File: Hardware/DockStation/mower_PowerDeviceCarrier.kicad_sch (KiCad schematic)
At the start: 5 parts, among them J1 Conn_01x04, J2 Conn_01x04

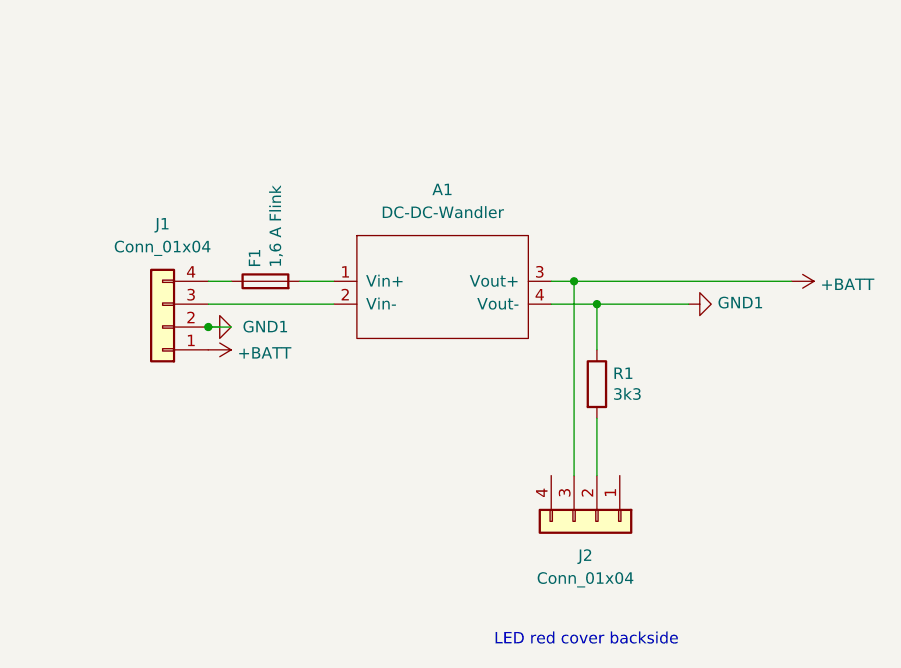
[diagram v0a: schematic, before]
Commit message: feat(dock): add 3.81mm terminals and pinholes to connect to dc/dc terminal
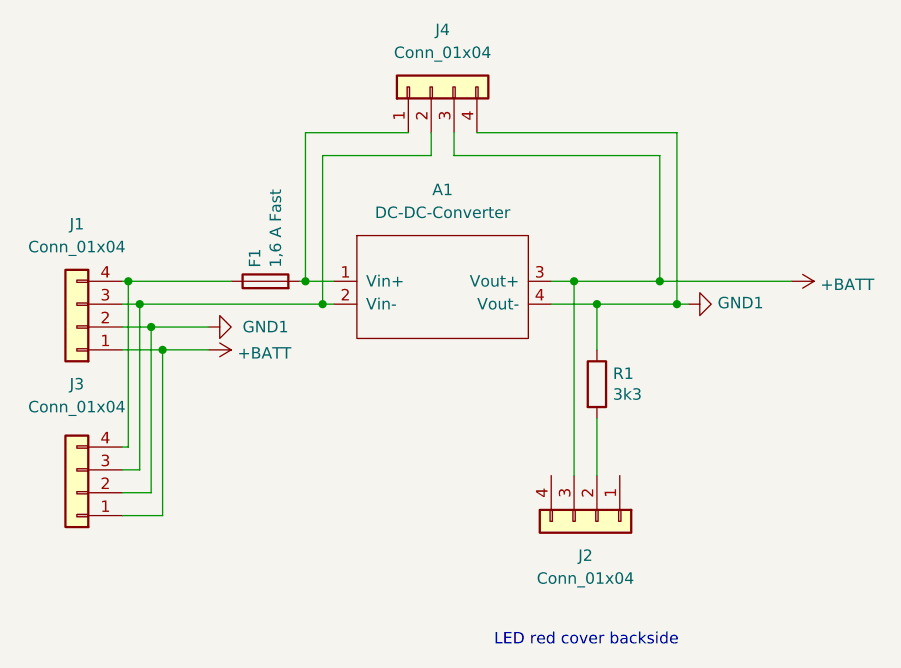
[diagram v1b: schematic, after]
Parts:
- added J3: Conn_01x04, Connector_Phoenix_MC:PhoenixContact_MCV_1,5_4-G-3.81_1x04_P3.81mm_Vertical, symbol ene9ba_library:Conn_01x04
- added J4: Conn_01x04, Connector_PinHeader_2.54mm:PinHeader_1x07_P2.54mm_Vertical, symbol Connector_Generic:Conn_01x04
- A1: value DC-DC-Wandler -> DC-DC-Converter
- F1: value 1,6 A Flink -> 1,6 A Fast
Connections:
- net +BATT: now also J3.1 (Pin_1), J4.3 (Pin_3)
- net GND1: now also J3.2 (Pin_2), J4.4 (Pin_4)
- net at F1.1, J1.4 (Pin_4): now also J3.4 (Pin_4)
- net at A1.1 (Vin+), F1.2: now also J4.1 (Pin_1)
- net at A1.2 (Vin-), J1.3 (Pin_3): now also J3.3 (Pin_3), J4.2 (Pin_2)
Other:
- moved on the sheet: J1
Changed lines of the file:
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@@
 (kicad_sch (version 20211123) (generator eeschema)
   (paper "A4")
+  (junction (at 100.33 77.47) (diameter 0) (color 0 0 0 0)
+  )
   (junction (at 151.13 77.47) (diameter 0) (color 0 0 0 0)
   )
+  (junction (at 99.06 74.93) (diameter 0) (color 0 0 0 0)
+  )
+  (junction (at 102.87 82.55) (diameter 0) (color 0 0 0 0)
+  )
+  (junction (at 120.65 77.47) (diameter 0) (color 0 0 0 0)
+  )
+  (junction (at 118.745 74.93) (diameter 0) (color 0 0 0 0)
+  )
+  (junction (at 160.02 77.47) (diameter 0) (color 0 0 0 0)
+  )
+  (junction (at 158.115 74.93) (diameter 0) (color 0 0 0 0)
+  )
   (junction (at 148.59 74.93) (diameter 0) (color 0 0 0 0)
   )
-  (junction (at 107.95 80.01) (diameter 0) (color 0 0 0 0)
+  (junction (at 101.6 80.01) (diameter 0) (color 0 0 0 0)
+  )
+  (wire (pts (xy 135.255 60.96) (xy 158.115 60.96))
+    (stroke (width 0) (type default) (color 0 0 0 0))
+  )
+  (wire (pts (xy 130.175 58.42) (xy 118.745 58.42))
+    (stroke (width 0) (type default) (color 0 0 0 0))
+  )
+  (wire (pts (xy 132.715 60.96) (xy 120.65 60.96))
+    (stroke (width 0) (type default) (color 0 0 0 0))
+  )
+  (wire (pts (xy 160.02 58.42) (xy 160.02 77.47))
+    (stroke (width 0) (type default) (color 0 0 0 0))
   )
   (wire (pts (xy 151.13 77.47) (xy 151.13 82.55))
     (stroke (width 0) (type default) (color 0 0 0 0))
   )
-  (wire (pts (xy 118.11 74.93) (xy 121.92 74.93))
-    (stroke (width 0) (type default) (color 0 0 0 0))
-  )
-  (wire (pts (xy 148.59 74.93) (xy 172.72 74.93))
+  (wire (pts (xy 118.11 74.93) (xy 118.745 74.93))
+    (stroke (width 0) (type default) (color 0 0 0 0))
+  )
+  (wire (pts (xy 98.425 98.425) (xy 101.6 98.425))
+    (stroke (width 0) (type default) (color 0 0 0 0))
+  )
+  (wire (pts (xy 148.59 74.93) (xy 158.115 74.93))
+    (stroke (width 0) (type default) (color 0 0 0 0))
+  )
+  (wire (pts (xy 100.33 95.885) (xy 100.33 77.47))
+    (stroke (width 0) (type default) (color 0 0 0 0))
+  )
+  (wire (pts (xy 98.425 100.965) (xy 102.87 100.965))
     (stroke (width 0) (type default) (color 0 0 0 0))
   )
@@
     (stroke (width 0) (type default) (color 0 0 0 0))
   )
-  (wire (pts (xy 107.95 74.93) (xy 110.49 74.93))
+  (wire (pts (xy 98.425 95.885) (xy 100.33 95.885))
+    (stroke (width 0) (type default) (color 0 0 0 0))
+  )
+  (wire (pts (xy 99.06 93.345) (xy 99.06 74.93))
+    (stroke (width 0) (type default) (color 0 0 0 0))
+  )
+  (wire (pts (xy 120.65 77.47) (xy 121.92 77.47))
+    (stroke (width 0) (type default) (color 0 0 0 0))
+  )
+  (wire (pts (xy 98.425 82.55) (xy 102.87 82.55))
+    (stroke (width 0) (type default) (color 0 0 0 0))
+  )
+  (wire (pts (xy 100.33 77.47) (xy 120.65 77.47))
+    (stroke (width 0) (type default) (color 0 0 0 0))
+  )
+  (wire (pts (xy 98.425 74.93) (xy 99.06 74.93))
+    (stroke (width 0) (type default) (color 0 0 0 0))
+  )
+  (wire (pts (xy 132.715 58.42) (xy 132.715 60.96))
     (stroke (width 0) (type default) (color 0 0 0 0))
   )
@@
     (stroke (width 0) (type default) (color 0 0 0 0))
   )
-  (wire (pts (xy 107.95 80.01) (xy 110.49 80.01))
-    (stroke (width 0) (type default) (color 0 0 0 0))
-  )
-  (wire (pts (xy 151.13 77.47) (xy 161.29 77.47))
+  (wire (pts (xy 99.06 74.93) (xy 110.49 74.93))
+    (stroke (width 0) (type default) (color 0 0 0 0))
+  )
+  (wire (pts (xy 158.115 60.96) (xy 158.115 74.93))
+    (stroke (width 0) (type default) (color 0 0 0 0))
+  )
+  (wire (pts (xy 135.255 58.42) (xy 135.255 60.96))
+    (stroke (width 0) (type default) (color 0 0 0 0))
+  )
+  (wire (pts (xy 120.65 60.96) (xy 120.65 77.47))
+    (stroke (width 0) (type default) (color 0 0 0 0))
+  )
+  (wire (pts (xy 98.425 80.01) (xy 101.6 80.01))
+    (stroke (width 0) (type default) (color 0 0 0 0))
+  )
+  (wire (pts (xy 101.6 80.01) (xy 107.95 80.01))
+    (stroke (width 0) (type default) (color 0 0 0 0))
+  )
+  (wire (pts (xy 102.87 82.55) (xy 107.95 82.55))
+    (stroke (width 0) (type default) (color 0 0 0 0))
+  )
+  (wire (pts (xy 151.13 77.47) (xy 160.02 77.47))
+    (stroke (width 0) (type default) (color 0 0 0 0))
+  )
+  (wire (pts (xy 158.115 74.93) (xy 172.72 74.93))
+    (stroke (width 0) (type default) (color 0 0 0 0))
+  )
+  (wire (pts (xy 137.795 58.42) (xy 160.02 58.42))
+    (stroke (width 0) (type default) (color 0 0 0 0))
+  )
+  (wire (pts (xy 101.6 98.425) (xy 101.6 80.01))
+    (stroke (width 0) (type default) (color 0 0 0 0))
+  )
+  (wire (pts (xy 102.87 100.965) (xy 102.87 82.55))
     (stroke (width 0) (type default) (color 0 0 0 0))
   )
@@
     (stroke (width 0) (type default) (color 0 0 0 0))
   )
-  (wire (pts (xy 107.95 77.47) (xy 121.92 77.47))
+  (wire (pts (xy 118.745 74.93) (xy 121.92 74.93))
+    (stroke (width 0) (type default) (color 0 0 0 0))
+  )
+  (wire (pts (xy 160.02 77.47) (xy 161.29 77.47))
+    (stroke (width 0) (type default) (color 0 0 0 0))
+  )
+  (wire (pts (xy 98.425 93.345) (xy 99.06 93.345))
+    (stroke (width 0) (type default) (color 0 0 0 0))
+  )
+  (wire (pts (xy 118.745 58.42) (xy 118.745 74.93))
+    (stroke (width 0) (type default) (color 0 0 0 0))
+  )
+  (wire (pts (xy 98.425 77.47) (xy 100.33 77.47))
     (stroke (width 0) (type default) (color 0 0 0 0))
   )
@@
       (effects (font (size 1.27 1.27)) (justify left))
     )
-    (property "Value" "1,6 A Flink" (id 1) (at 115.443 73.406 0)
+    (property "Value" "1,6 A Fast" (id 1) (at 115.443 73.406 0)
       (effects (font (size 1.27 1.27)) (justify left))
     )
@@
     (pin "1")
   )
-  (symbol (lib_id "ene9ba_library:Conn_01x04") (at 102.87 80.01 180) (unit 1)
-    (in_bom yes) (on_board yes) (fields_autoplaced)
-    (property "Reference" "J1" (id 0) (at 102.87 68.58 0))
-    (property "Value" "Conn_01x04" (id 1) (at 102.87 71.12 0))
-    (property "Footprint" "Connector_Phoenix_MSTB:PhoenixContact_MSTBVA_2,5_4-G-5,08_1x04_P5.08mm_Vertical" (id 2) (at 102.87 80.01 0)
-      (effects (font (size 1.27 1.27)) hide)
-    )
-    (property "Datasheet" "" (id 3) (at 102.87 80.01 0)
+  (symbol (lib_id "ene9ba_library:Conn_01x04") (at 93.345 98.425 180) (unit 1)
+    (in_bom yes) (on_board yes) (fields_autoplaced)
+    (property "Reference" "J3" (id 0) (at 93.345 86.36 0))
+    (property "Value" "Conn_01x04" (id 1) (at 93.345 88.9 0))
+    (property "Footprint" "Connector_Phoenix_MC:PhoenixContact_MCV_1,5_4-G-3.81_1x04_P3.81mm_Vertical" (id 2) (at 93.345 98.425 0)
+      (effects (font (size 1.27 1.27)) hide)
+    )
+    (property "Datasheet" "" (id 3) (at 93.345 98.425 0)
+      (effects (font (size 1.27 1.27)) hide)
+    )
+    (pin "1")
+    (pin "2")
+    (pin "3")
+    (pin "4")
+  )
+  (symbol (lib_id "Connector_Generic:Conn_01x04") (at 132.715 53.34 90) (unit 1)
+    (in_bom yes) (on_board yes) (fields_autoplaced)
+    (property "Reference" "J4" (id 0) (at 133.985 46.99 90))
+    (property "Value" "Conn_01x04" (id 1) (at 133.985 49.53 90))
+    (property "Footprint" "Connector_PinHeader_2.54mm:PinHeader_1x07_P2.54mm_Vertical" (id 2) (at 132.715 53.34 0)
+      (effects (font (size 1.27 1.27)) hide)
+    )
+    (property "Datasheet" "~" (id 3) (at 132.715 53.34 0)
+      (effects (font (size 1.27 1.27)) hide)
+    )
+    (pin "1")
+    (pin "2")
+    (pin "3")
+    (pin "4")
+  )
+  (symbol (lib_id "ene9ba_library:Conn_01x04") (at 93.345 80.01 180) (unit 1)
+    (in_bom yes) (on_board yes) (fields_autoplaced)
+    (property "Reference" "J1" (id 0) (at 93.345 68.58 0))
+    (property "Value" "Conn_01x04" (id 1) (at 93.345 71.12 0))
+    (property "Footprint" "Connector_Phoenix_MSTB:PhoenixContact_MSTBVA_2,5_4-G-5,08_1x04_P5.08mm_Vertical" (id 2) (at 93.345 80.01 0)
+      (effects (font (size 1.27 1.27)) hide)
+    )
+    (property "Datasheet" "" (id 3) (at 93.345 80.01 0)
       (effects (font (size 1.27 1.27)) hide)
     )
@@
     (in_bom yes) (on_board yes) (fields_autoplaced)
     (property "Reference" "A1" (id 0) (at 133.985 64.77 0))
-    (property "Value" "DC-DC-Wandler" (id 1) (at 133.985 67.31 0))
+    (property "Value" "DC-DC-Converter" (id 1) (at 133.985 67.31 0))
     (property "Footprint" "ene9ba_footprint:DC-DC-XL4016" (id 2) (at 124.46 82.55 0)
       (effects (font (size 1.27 1.27)) hide)
@@
     )
     (path "/fc93bf9c-6b77-45fa-9005-5264c25cd164"
-      (reference "A1") (unit 1) (value "DC-DC-Wandler") (footprint "ene9ba_footprint:DC-DC-XL4016")
+      (reference "A1") (unit 1) (value "DC-DC-Converter") (footprint "ene9ba_footprint:DC-DC-XL4016")
     )
     (path "/00000000-0000-0000-0000-000061321fb3"
-      (reference "F1") (unit 1) (value "1,6 A Flink") (footprint "ene9ba_footprint:Fuseholder5x20_horiz_open_inline_Type-I")
+      (reference "F1") (unit 1) (value "1,6 A Fast") (footprint "ene9ba_footprint:Fuseholder5x20_horiz_open_inline_Type-I")
     )
     (path "/e3e397bf-a825-49de-839d-d13535924514"
@@
       (reference "J2") (unit 1) (value "Conn_01x04") (footprint "ene9ba_footprint:PinHeader_1x04_P2.54mm_Horizontal")
     )
+    (path "/018f5e16-b12c-4dd5-8959-93c7fb2224b4"
+      (reference "J3") (unit 1) (value "Conn_01x04") (footprint "Connector_Phoenix_MC:PhoenixContact_MCV_1,5_4-G-3.81_1x04_P3.81mm_Vertical")
+    )
+    (path "/c4135068-a1fe-4a06-87a3-bf5da63ae625"
+      (reference "J4") (unit 1) (value "Conn_01x04") (footprint "Connector_PinHeader_2.54mm:PinHeader_1x07_P2.54mm_Vertical")
+    )
     (path "/00000000-0000-0000-0000-00006133ba70"

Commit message: fix(dock): erc/drc
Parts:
- J4: symbol Connector_Generic:Conn_01x04 -> Connector:Conn_01x04_Female
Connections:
- no-connect marks 0 -> 2
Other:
- moved on the sheet: F1
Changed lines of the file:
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@@
   (junction (at 101.6 80.01) (diameter 0) (color 0 0 0 0)
   )
+  (no_connect (at 146.05 96.52))
+  (no_connect (at 153.67 96.52))
   (wire (pts (xy 135.255 60.96) (xy 158.115 60.96))
     (stroke (width 0) (type default) (color 0 0 0 0))
@@
     (stroke (width 0) (type default) (color 0 0 0 0))
   )
-  (wire (pts (xy 118.11 74.93) (xy 118.745 74.93))
+  (wire (pts (xy 116.84 74.93) (xy 118.745 74.93))
     (stroke (width 0) (type default) (color 0 0 0 0))
   )
@@
     (stroke (width 0) (type default) (color 0 0 0 0))
   )
-  (wire (pts (xy 99.06 74.93) (xy 110.49 74.93))
+  (wire (pts (xy 99.06 74.93) (xy 109.22 74.93))
     (stroke (width 0) (type default) (color 0 0 0 0))
   )
@@
     (effects (font (size 1.27 1.27)) (justify left bottom))
   )
-  (symbol (lib_id "Device:Fuse") (at 114.3 74.93 90) (unit 1)
-    (in_bom yes) (on_board yes)
-    (property "Reference" "F1" (id 0) (at 113.1316 73.406 0)
-      (effects (font (size 1.27 1.27)) (justify left))
-    )
-    (property "Value" "1,6 A Fast" (id 1) (at 115.443 73.406 0)
-      (effects (font (size 1.27 1.27)) (justify left))
-    )
-    (property "Footprint" "ene9ba_footprint:Fuseholder5x20_horiz_open_inline_Type-I" (id 2) (at 114.3 76.708 90)
-      (effects (font (size 1.27 1.27)) hide)
-    )
-    (property "Datasheet" "~" (id 3) (at 114.3 74.93 0)
+  (symbol (lib_id "Device:Fuse") (at 113.03 74.93 90) (unit 1)
+    (in_bom yes) (on_board yes)
+    (property "Reference" "F1" (id 0) (at 111.506 76.0984 0)
+      (effects (font (size 1.27 1.27)) (justify left))
+    )
+    (property "Value" "1,6 A Fast" (id 1) (at 111.506 73.787 0)
+      (effects (font (size 1.27 1.27)) (justify left))
+    )
+    (property "Footprint" "ene9ba_footprint:Fuseholder5x20_horiz_open_inline_Type-I" (id 2) (at 115.57 71.12 90)
+      (effects (font (size 1.27 1.27)) hide)
+    )
+    (property "Datasheet" "~" (id 3) (at 113.03 74.93 0)
       (effects (font (size 1.27 1.27)) hide)
     )
@@
     (pin "4")
   )
-  (symbol (lib_id "Connector_Generic:Conn_01x04") (at 132.715 53.34 90) (unit 1)
+  (symbol (lib_id "Connector:Conn_01x04_Female") (at 132.715 53.34 90) (unit 1)
     (in_bom yes) (on_board yes) (fields_autoplaced)
     (property "Reference" "J4" (id 0) (at 133.985 46.99 90))
@@
     (pin "4")
   )
-  (symbol (lib_id "ene9ba_library:Conn_01x04") (at 93.345 80.01 180) (unit 1)
-    (in_bom yes) (on_board yes) (fields_autoplaced)
-    (property "Reference" "J1" (id 0) (at 93.345 68.58 0))
-    (property "Value" "Conn_01x04" (id 1) (at 93.345 71.12 0))
-    (property "Footprint" "Connector_Phoenix_MSTB:PhoenixContact_MSTBVA_2,5_4-G-5,08_1x04_P5.08mm_Vertical" (id 2) (at 93.345 80.01 0)
+  (symbol (lib_name "Conn_01x04_1") (lib_id "ene9ba_library:Conn_01x04") (at 93.345 80.01 180) (unit 1)
+    (in_bom yes) (on_board yes) (fields_autoplaced)
+    (property "Reference" "J1" (id 0) (at 93.345 91.44 0))
+    (property "Value" "Conn_01x04" (id 1) (at 93.345 88.9 0))
+    (property "Footprint" "Connector_Phoenix_MSTB:PhoenixContact_MSTBVA_2,5_4-G-5,08_1x04_P5.08mm_Vertical" (id 2) (at 93.345 71.12 0)
       (effects (font (size 1.27 1.27)) hide)
     )
@@
       (effects (font (size 1.27 1.27)) hide)
     )
-    (property "Datasheet" "/home/ene9ba/project/Git/OpenMowerPrivate/PowerDeviceCarrier/mower_PowerDeviceCarrier_V2/XL4016_Step_Down_Buck_DC_DC_Converter.pdf" (id 3) (at 124.46 82.55 0)
-      (effects (font (size 1.27 1.27)) hide)
-    )
+    (property "Datasheet" "" (id 3) (at 124.46 82.55 0)
+      (effects (font (size 1.27 1.27)) hide)
+    )
